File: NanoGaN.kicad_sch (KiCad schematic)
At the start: 20 parts, among them J1 XT60-M, J2 XT60-M, J3 Phase_U, J4 Phase_V, J5 Phase_W

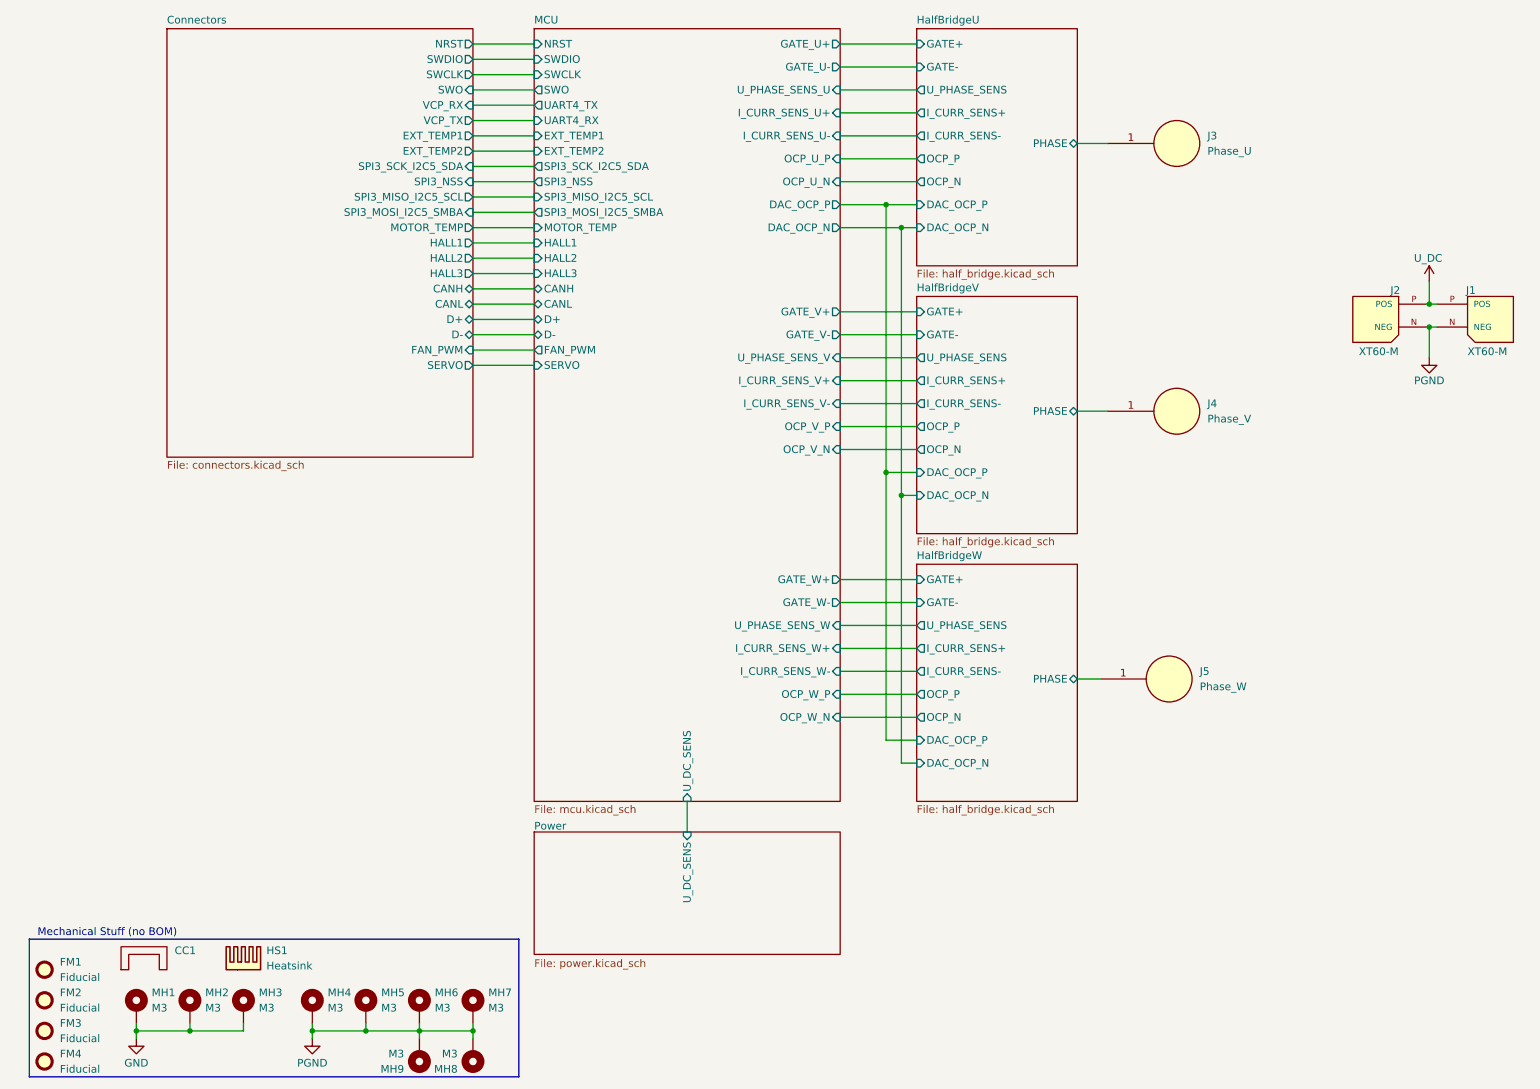
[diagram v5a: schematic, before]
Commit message: ERC errors have been fixed. XTAL changed to 12MHz. WiP DRC errors.
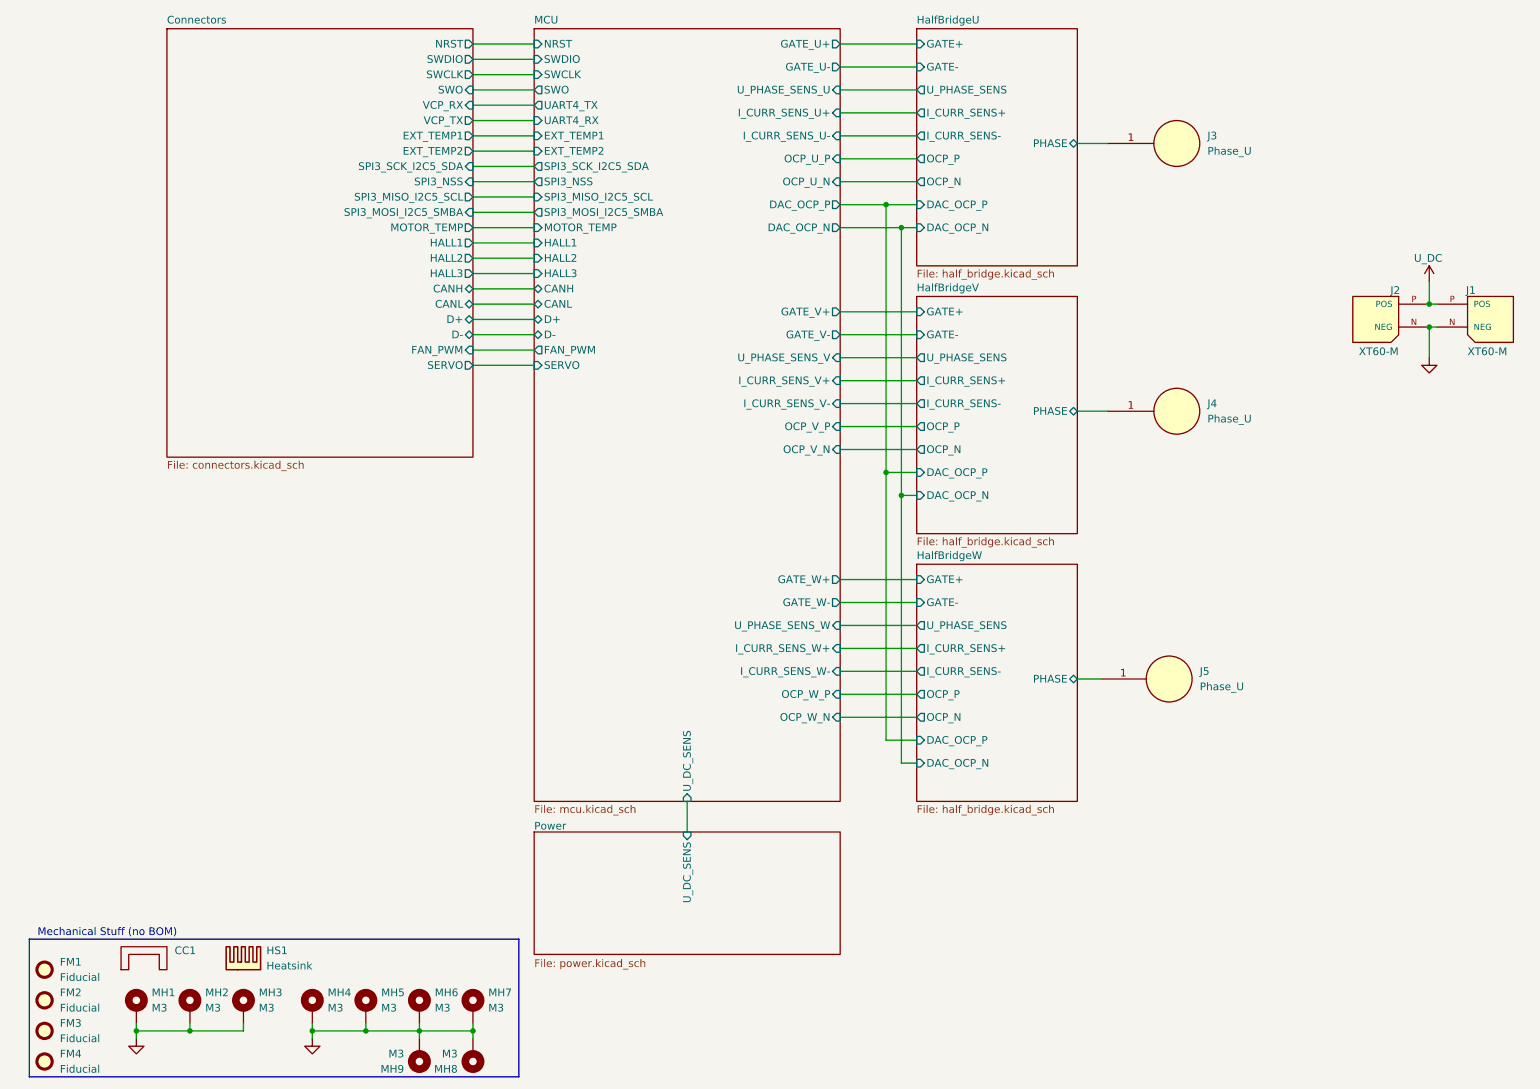
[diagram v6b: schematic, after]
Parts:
- removed J3: Phase_U, TerminalBlock_Wuerth:Wuerth_REDCUBE-THR_WP-THRBU_74650073_THR, symbol Connector_Generic:Power_Welding_PAD
- removed J4: Phase_V, TerminalBlock_Wuerth:Wuerth_REDCUBE-THR_WP-THRBU_74650073_THR, symbol Connector_Generic:Power_Welding_PAD
- removed J5: Phase_W, TerminalBlock_Wuerth:Wuerth_REDCUBE-THR_WP-THRBU_74650073_THR, symbol Connector_Generic:Power_Welding_PAD
- added J3, J4, J5: Phase_U, TerminalBlock_Wuerth:Wuerth_REDCUBE-THR_WP-THRBU_74650073_THR, symbol NanoGaN:Power_Welding_PAD
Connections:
- net PGND is gone; now on net GND: J1.N (NEG), J2.N (NEG), MH4.1, MH5.1, MH6.1, MH7.1, MH8.1, MH9.1
- net HalfBridgeU/PHASE: now also J3.1
- net HalfBridgeV/PHASE: now also J4.1
- net HalfBridgeW/PHASE: now also J5.1

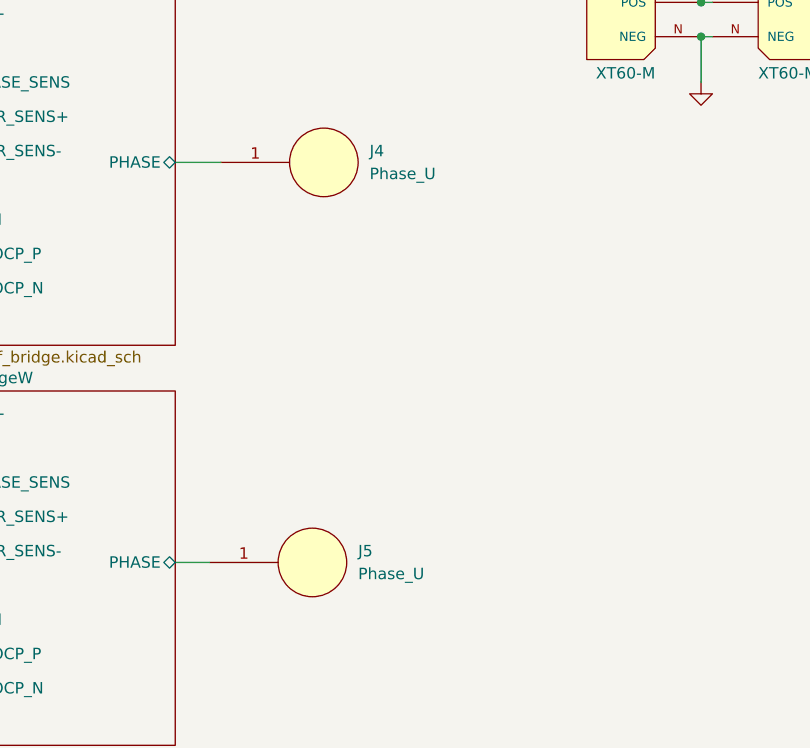
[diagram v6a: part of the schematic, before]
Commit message: fixed all ERC and DRC errors/warnings, now in review stage.
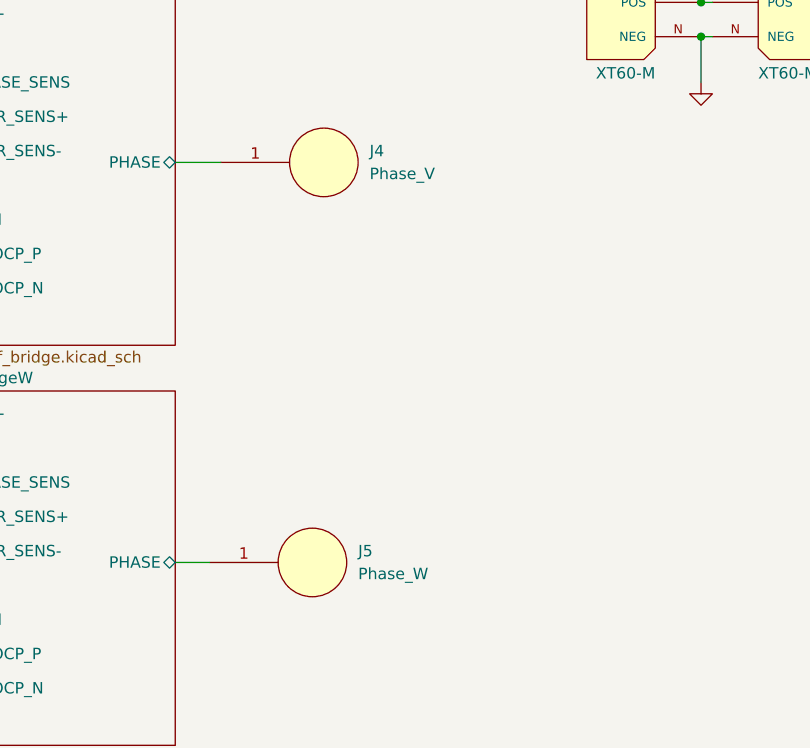
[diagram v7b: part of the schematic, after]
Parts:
- J4: value Phase_U -> Phase_V
- J5: value Phase_U -> Phase_W
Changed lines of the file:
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@@
 			)
 		)
-		(property "Value" "Phase_U"
+		(property "Value" "Phase_W"
 			(at 209.55 130.8099 0)
 			(effects
@@
 			)
 		)
-		(property "Value" "Phase_U"
+		(property "Value" "Phase_V"
 			(at 210.82 86.3599 0)
 			(effects

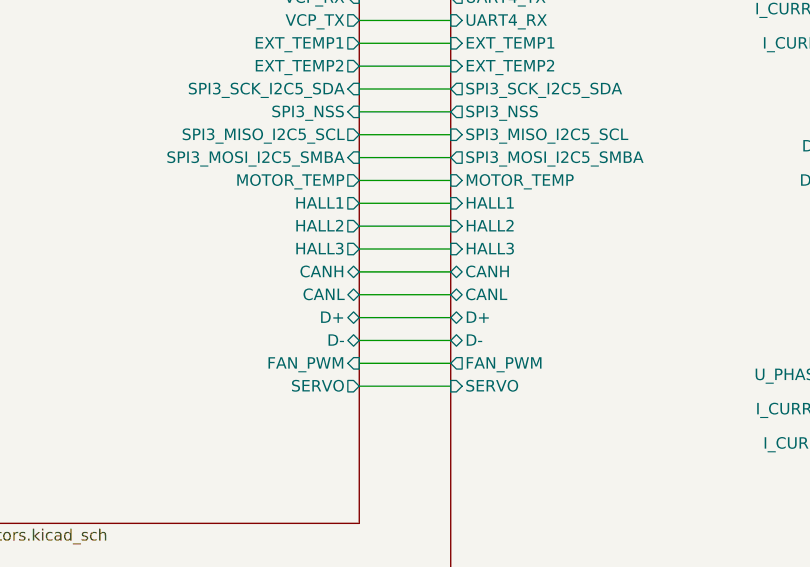
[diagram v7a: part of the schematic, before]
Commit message: added leds and buttons
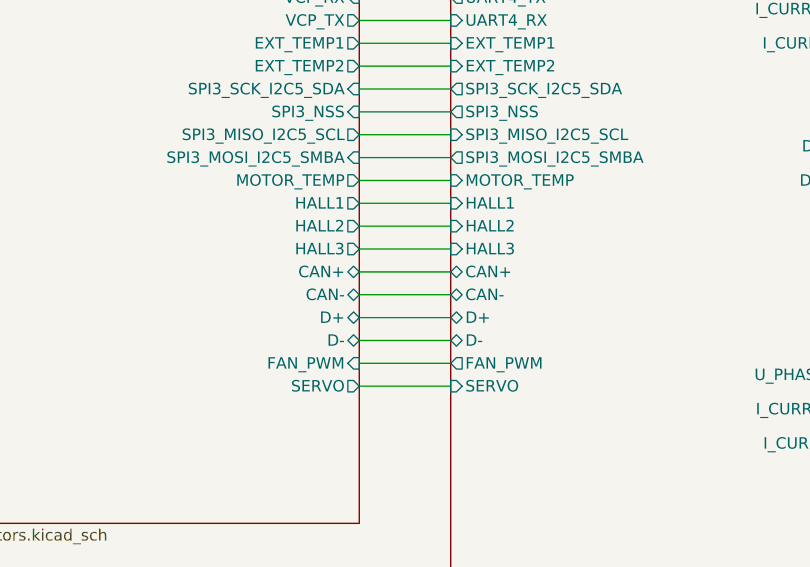
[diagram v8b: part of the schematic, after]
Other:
- sheet Connectors ports: added CAN+, CAN-; removed CANH, CANL
- sheet MCU ports: added CAN+, CAN-; removed CANH, CANL
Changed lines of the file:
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@@
-			)
-		)
-		(pin "CANH" bidirectional
-			(at 88.9 64.77 0)
-			(effects
-				(font
-					(size 1.27 1.27)
-				)
-				(justify right)
-			)
-		)
-		(pin "CANL" bidirectional
-			(at 88.9 67.31 0)
-			(effects
-				(font
-					(size 1.27 1.27)
-				)
-				(justify right)
 			)
 		)
@@
 		(pin "SERVO" output
 			(at 88.9 77.47 0)
+			(effects
+				(font
+					(size 1.27 1.27)
+				)
+				(justify right)
+			)
+		)
+		(pin "CAN+" bidirectional
+			(at 88.9 64.77 0)
+			(effects
+				(font
+					(size 1.27 1.27)
+				)
+				(justify right)
+			)
+		)
+		(pin "CAN-" bidirectional
+			(at 88.9 67.31 0)
 			(effects
 				(font
@@
 			)
 		)
-		(pin "CANH" bidirectional
-			(at 99.06 64.77 180)
-			(effects
-				(font
-					(size 1.27 1.27)
-				)
-				(justify left)
-			)
-		)
-		(pin "CANL" bidirectional
-			(at 99.06 67.31 180)
-			(effects
-				(font
-					(size 1.27 1.27)
-				)
-				(justify left)
-			)
-		)
 		(pin "D-" bidirectional
 			(at 99.06 72.39 180)
@@
 			(effects
 				(font
+					(size 1.27 1.27)
+				)
+				(justify left)
+			)
+		)
+		(pin "CAN+" bidirectional
+			(at 99.06 64.77 180)
+			(effects
+				(font
+					(size 1.27 1.27)
+				)
+				(justify left)
+			)
+		)
+		(pin "CAN-" bidirectional
+			(at 99.06 67.31 180)
+			(effects
+				(font
